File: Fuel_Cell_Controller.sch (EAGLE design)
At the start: 54 parts, among them U1 MAX232PTH

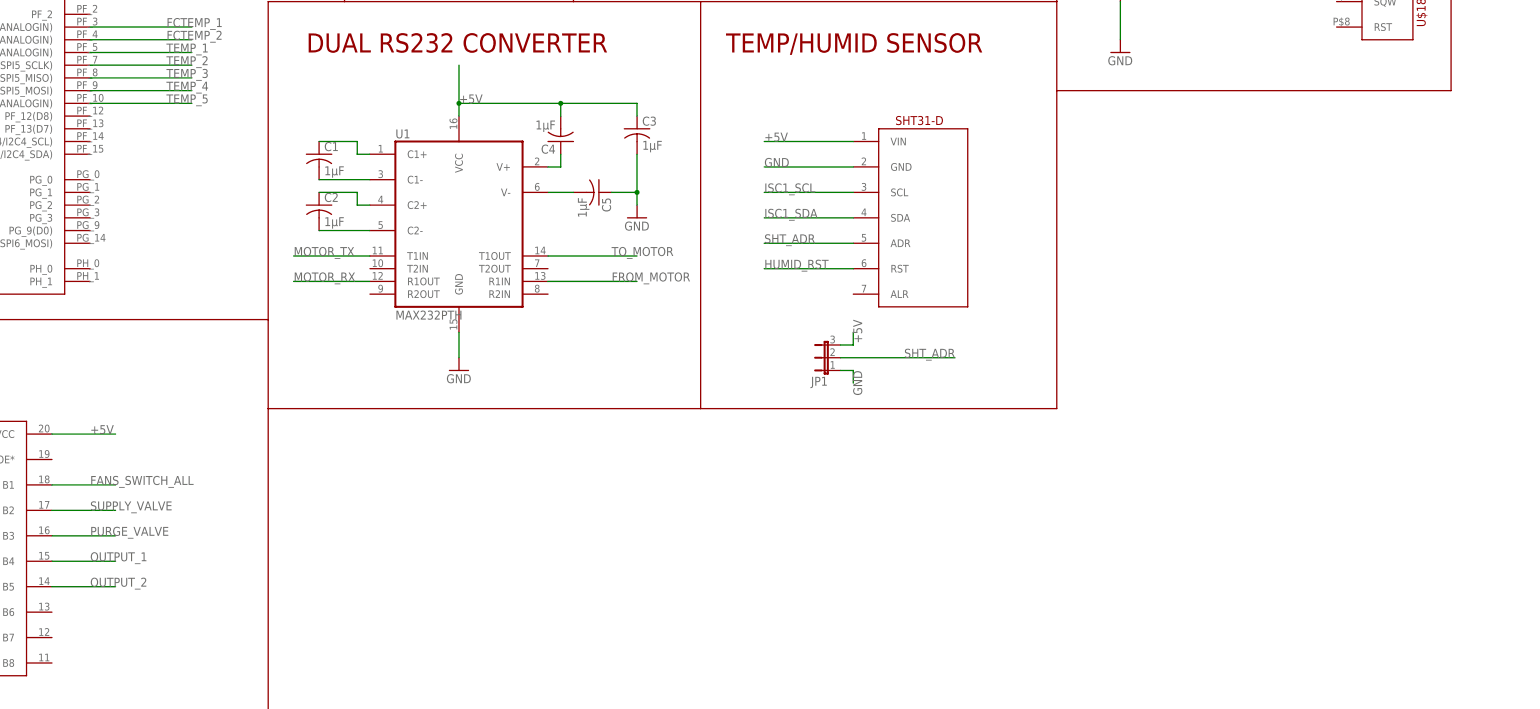
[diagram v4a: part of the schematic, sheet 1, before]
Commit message: Added ADC to schematic
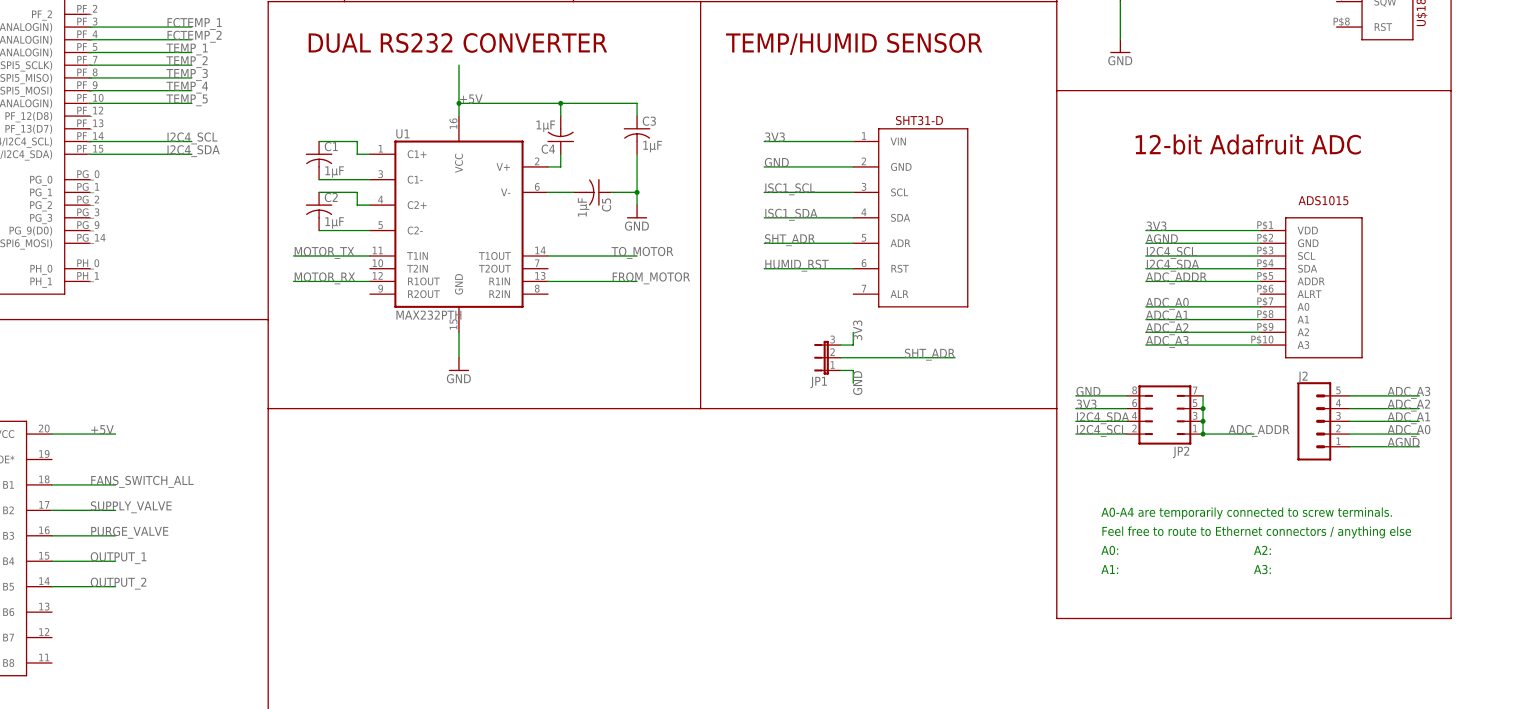
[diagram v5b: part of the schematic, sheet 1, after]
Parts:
- added J2: (no value), SparkFun-Connectors:CONN_05SCREW
- added JP2: (no value), jumper:JP4Q
- added U$19: ADS1015, FCC_parts:ADS1015
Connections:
- new net ADC_A0: J2.2, U$19.A0
- new net ADC_A1: J2.3, U$19.A1
- new net ADC_A2: J2.4, U$19.A2
- new net ADC_A3: J2.5, U$19.A3
- new net ADC_ADDR: JP2.1, JP2.3, JP2.5, JP2.7, U$19.ADDR
- new net I2C4_SCL: JP2.2, U$1.PF_14(D4/I2C4_SCL), U$19.SCL
- new net I2C4_SDA: JP2.4, U$1.PF_15(D2/I2C4_SDA), U$19.SDA
- net +5V: no longer JP1.3, SHTSENSOR.VIN
- net 3V3: now also JP1.3, JP2.6, SHTSENSOR.VIN, U$19.VDD
- net AGND: now also J2.1, U$19.GND
- net GND: now also JP2.8
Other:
- note added: "12-bit Adafruit ADC"
- note added: "A0-A4 are temporarily connected to screw terminals."
- note added: "A0:"
- note added: "A1:"
- note added: "A2:"
- note added: "A3:"
- note added: "Feel free to route to Ethernet connectors / anything else"
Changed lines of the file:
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@@
 <?xml version="1.0" encoding="utf-8"?>
 <!DOCTYPE eagle SYSTEM "eagle.dtd">
-<eagle version="8.4.0">
+<eagle version="8.3.2">
 <drawing>
 <settings>
@@
 <setting verticaltext="up"/>
 </settings>
-<grid distance="0.1" unitdist="inch" unit="inch" style="lines" multiple="1" display="no" altdistance="0.01" altunitdist="inch" altunit="inch"/>
+<grid distance="0.05" unitdist="inch" unit="inch" style="dots" multiple="1" display="no" altdistance="0.005" altunitdist="inch" altunit="inch"/>
 <layers>
 <layer number="1" name="Top" color="4" fill="1" visible="no" active="no"/>
@@
 <part name="C6" library="SparkFun-Capacitors" deviceset="CAP" device="0603-CAP"/>
 <part name="GND4" library="E-P-008-R1.2" deviceset="GND" device=""/>
+<part name="U$19" library="FCC_parts" deviceset="ADS1015" device=""/>
+<part name="JP2" library="jumper" library_urn="urn:adsk.eagle:library:252" deviceset="JP4Q" device="" package3d_urn="urn:adsk.eagle:package:15451/1"/>
+<part name="J2" library="SparkFun-Connectors" library_urn="urn:adsk.eagle:library:513" deviceset="CONN_05" device="SCREW" package3d_urn="urn:adsk.eagle:package:38112/1"/>
 </parts>
 <sheets>
@@
 <wire x1="-93.98" y1="-78.74" x2="124.46" y2="-78.74" width="0.1524" layer="94"/>
 <text x="-10.16" y="-88.9" size="3.81" layer="94">OUTPUT BUFFERS</text>
+<text x="297.18" y="-45.72" size="3.81" layer="94">12-bit Adafruit ADC</text>
+<wire x1="281.94" y1="-96.52" x2="281.94" y2="-138.43" width="0.2032" layer="94"/>
+<wire x1="281.94" y1="-138.43" x2="360.68" y2="-138.43" width="0.2032" layer="94"/>
+<wire x1="360.68" y1="-138.43" x2="360.68" y2="-33.02" width="0.2032" layer="94"/>
+<text x="290.83" y="-118.11" size="1.778" layer="91">A0-A4 are temporarily connected to screw terminals.</text>
+<text x="290.83" y="-121.92" size="1.778" layer="91">Feel free to route to Ethernet connectors / anything else</text>
+<text x="290.83" y="-125.73" size="1.778" layer="91">A0:</text>
+<text x="290.83" y="-129.54" size="1.778" layer="91">A1:</text>
+<text x="321.31" y="-125.73" size="1.778" layer="91">A2:</text>
+<text x="321.31" y="-129.54" size="1.778" layer="91">A3:</text>
 </plain>
 <instances>
@@
 <instance part="C6" gate="G$1" x="294.64" y="-12.7"/>
 <instance part="GND4" gate="1" x="294.64" y="-25.4"/>
+<instance part="U$19" gate="G$1" x="322.58" y="-81.28"/>
+<instance part="JP2" gate="B" x="303.53" y="-99.06" rot="R90"/>
+<instance part="J2" gate="G$1" x="332.74" y="-99.06"/>
 </instances>
 <busses>
@@
 <wire x1="294.64" y1="-15.24" x2="294.64" y2="-22.86" width="0.1524" layer="91"/>
 <pinref part="GND4" gate="1" pin="GND"/>
+</segment>
+<segment>
+<pinref part="JP2" gate="B" pin="8"/>
+<wire x1="295.91" y1="-93.98" x2="285.75" y2="-93.98" width="0.1524" layer="91"/>
+<label x="285.75" y="-93.98" size="1.778" layer="95"/>
 </segment>
 </net>
@@
 <wire x1="-12.7" y1="-101.6" x2="2.54" y2="-101.6" width="0.1524" layer="91"/>
 <label x="-2.54" y="-101.6" size="1.778" layer="95"/>
-</segment>
-<segment>
-<pinref part="SHTSENSOR" gate="G$1" pin="VIN"/>
-<wire x1="241.3" y1="-43.18" x2="223.52" y2="-43.18" width="0.1524" layer="91"/>
-<label x="223.52" y="-43.18" size="1.778" layer="95"/>
-</segment>
-<segment>
-<pinref part="JP1" gate="1" pin="3"/>
-<wire x1="238.76" y1="-83.82" x2="241.3" y2="-83.82" width="0.1524" layer="91"/>
-<wire x1="241.3" y1="-83.82" x2="241.3" y2="-81.28" width="0.1524" layer="91"/>
-<label x="241.3" y="-78.74" size="1.778" layer="95" rot="R270"/>
 </segment>
 <segment>
@@
 <junction x="294.64" y="2.54"/>
 </segment>
+<segment>
+<pinref part="SHTSENSOR" gate="G$1" pin="VIN"/>
+<wire x1="241.3" y1="-43.18" x2="223.52" y2="-43.18" width="0.1524" layer="91"/>
+<label x="223.52" y="-43.18" size="1.778" layer="95"/>
+</segment>
+<segment>
+<pinref part="JP1" gate="1" pin="3"/>
+<wire x1="238.76" y1="-83.82" x2="241.3" y2="-83.82" width="0.1524" layer="91"/>
+<wire x1="241.3" y1="-83.82" x2="241.3" y2="-81.28" width="0.1524" layer="91"/>
+<label x="241.3" y="-78.74" size="1.778" layer="95" rot="R270"/>
+</segment>
+<segment>
+<pinref part="U$19" gate="G$1" pin="VDD"/>
+<wire x1="322.58" y1="-60.96" x2="299.72" y2="-60.96" width="0.1524" layer="91"/>
+<label x="299.72" y="-60.96" size="1.778" layer="95"/>
+</segment>
+<segment>
+<pinref part="JP2" gate="B" pin="6"/>
+<wire x1="295.91" y1="-96.52" x2="285.75" y2="-96.52" width="0.1524" layer="91"/>
+<label x="285.75" y="-96.52" size="1.778" layer="95"/>
+</segment>
 </net>
 <net name="OPEN_RST" class="0">
@@
 <label x="-81.28" y="30.48" size="1.778" layer="95"/>
 </segment>
+<segment>
+<pinref part="U$19" gate="G$1" pin="GND"/>
+<wire x1="322.58" y1="-63.5" x2="299.72" y2="-63.5" width="0.1524" layer="91"/>
+<label x="299.72" y="-63.5" size="1.778" layer="95"/>
+</segment>
+<segment>
+<pinref part="J2" gate="G$1" pin="1"/>
+<wire x1="340.36" y1="-104.14" x2="354.33" y2="-104.14" width="0.1524" layer="91"/>
+<label x="347.98" y="-104.14" size="1.778" layer="95"/>
+</segment>
 </net>
 <net name="MASS_FLOW" class="0">
@@
 </segment>
 </net>
+<net name="ADC_A0" class="0">
+<segment>
+<pinref part="U$19" gate="G$1" pin="A0"/>
+<wire x1="322.58" y1="-76.2" x2="299.72" y2="-76.2" width="0.1524" layer="91"/>
+<label x="299.72" y="-76.2" size="1.778" layer="95"/>
+</segment>
+<segment>
+<pinref part="J2" gate="G$1" pin="2"/>
+<wire x1="340.36" y1="-101.6" x2="354.33" y2="-101.6" width="0.1524" layer="91"/>
+<label x="347.98" y="-101.6" size="1.778" layer="95"/>
+</segment>
+</net>
+<net name="ADC_A1" class="0">
+<segment>
+<pinref part="U$19" gate="G$1" pin="A1"/>
+<wire x1="322.58" y1="-78.74" x2="299.72" y2="-78.74" width="0.1524" layer="91"/>
+<label x="299.72" y="-78.74" size="1.778" layer="95"/>
+</segment>
+<segment>
+<pinref part="J2" gate="G$1" pin="3"/>
+<wire x1="340.36" y1="-99.06" x2="354.33" y2="-99.06" width="0.1524" layer="91"/>
+<label x="347.98" y="-99.06" size="1.778" layer="95"/>
+</segment>
+</net>
+<net name="ADC_A2" class="0">
+<segment>
+<pinref part="U$19" gate="G$1" pin="A2"/>
+<wire x1="322.58" y1="-81.28" x2="299.72" y2="-81.28" width="0.1524" layer="91"/>
+<label x="299.72" y="-81.28" size="1.778" layer="95"/>
+</segment>
+<segment>
+<pinref part="J2" gate="G$1" pin="4"/>
+<wire x1="340.36" y1="-96.52" x2="354.33" y2="-96.52" width="0.1524" layer="91"/>
+<label x="347.98" y="-96.52" size="1.778" layer="95"/>
+</segment>
+</net>
+<net name="ADC_A3" class="0">
+<segment>
+<pinref part="U$19" gate="G$1" pin="A3"/>
+<wire x1="322.58" y1="-83.82" x2="299.72" y2="-83.82" width="0.1524" layer="91"/>
+<label x="299.72" y="-83.82" size="1.778" layer="95"/>
+</segment>
+<segment>
+<pinref part="J2" gate="G$1" pin="5"/>
+<wire x1="340.36" y1="-93.98" x2="354.33" y2="-93.98" width="0.1524" layer="91"/>
+<label x="347.98" y="-93.98" size="1.778" layer="95"/>
+</segment>
+</net>
+<net name="I2C4_SCL" class="0">
+<segment>
+<pinref part="U$1" gate="G$1" pin="PF_14(D4/I2C4_SCL)"/>
+<wire x1="88.9" y1="-43.18" x2="109.22" y2="-43.18" width="0.1524" layer="91"/>
+<label x="104.14" y="-43.18" size="1.778" layer="95"/>
+</segment>
+<segment>
+<pinref part="U$19" gate="G$1" pin="SCL"/>
+<wire x1="322.58" y1="-66.04" x2="299.72" y2="-66.04" width="0.1524" layer="91"/>
+<label x="299.72" y="-66.04" size="1.778" layer="95"/>
+</segment>
+<segment>
+<pinref part="JP2" gate="B" pin="2"/>
+<wire x1="295.91" y1="-101.6" x2="285.75" y2="-101.6" width="0.1524" layer="91"/>
+<label x="285.75" y="-101.6" size="1.778" layer="95"/>
+</segment>
+</net>
+<net name="I2C4_SDA" class="0">
+<segment>
+<pinref part="U$1" gate="G$1" pin="PF_15(D2/I2C4_SDA)"/>
+<wire x1="88.9" y1="-45.72" x2="109.22" y2="-45.72" width="0.1524" layer="91"/>
+<label x="104.14" y="-45.72" size="1.778" layer="95"/>
+</segment>
+<segment>
+<pinref part="U$19" gate="G$1" pin="SDA"/>
+<wire x1="322.58" y1="-68.58" x2="299.72" y2="-68.58" width="0.1524" layer="91"/>
+<label x="299.72" y="-68.58" size="1.778" layer="95"/>
+</segment>
+<segment>
+<pinref part="JP2" gate="B" pin="4"/>
+<wire x1="295.91" y1="-99.06" x2="285.75" y2="-99.06" width="0.1524" layer="91"/>
+<label x="285.75" y="-99.06" size="1.778" layer="95"/>
+</segment>
+</net>
+<net name="ADC_ADDR" class="0">
+<segment>
+<pinref part="JP2" gate="B" pin="7"/>
+<pinref part="JP2" gate="B" pin="5"/>
+<wire x1="311.15" y1="-93.98" x2="311.15" y2="-96.52" width="0.1524" layer="91"/>
+<pinref part="JP2" gate="B" pin="3"/>
+<wire x1="311.15" y1="-96.52" x2="311.15" y2="-99.06" width="0.1524" layer="91"/>
+<junction x="311.15" y="-96.52"/>
+<pinref part="JP2" gate="B" pin="1"/>
+<wire x1="311.15" y1="-99.06" x2="311.15" y2="-101.6" width="0.1524" layer="91"/>
+<junction x="311.15" y="-99.06"/>
+<wire x1="311.15" y1="-101.6" x2="321.31" y2="-101.6" width="0.1524" layer="91"/>
+<junction x="311.15" y="-101.6"/>
+<label x="316.23" y="-101.6" size="1.778" layer="95"/>
+</segment>
+<segment>
+<pinref part="U$19" gate="G$1" pin="ADDR"/>
+<wire x1="322.58" y1="-71.12" x2="299.72" y2="-71.12" width="0.1524" layer="91"/>
+<label x="299.72" y="-71.12" size="1.778" layer="95"/>
+</segment>
+</net>

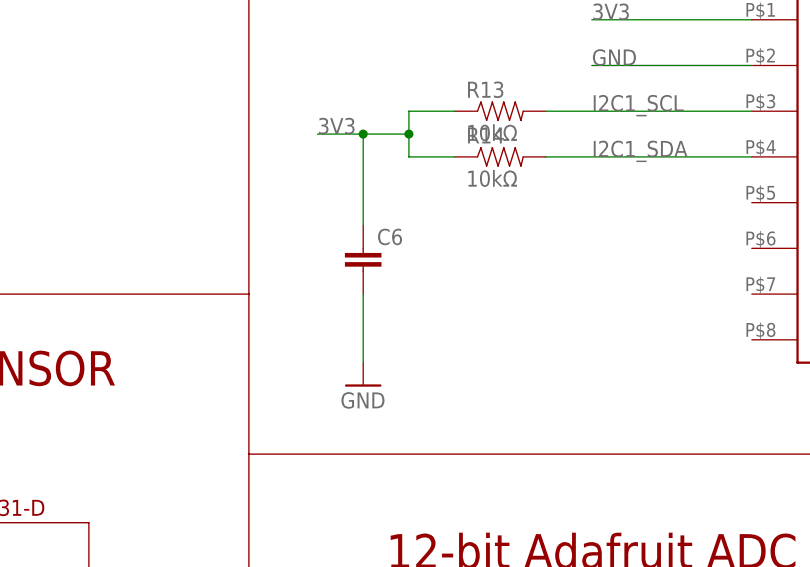
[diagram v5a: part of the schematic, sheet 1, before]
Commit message: Added value for capacitor between 3v3 and gnd on rtc
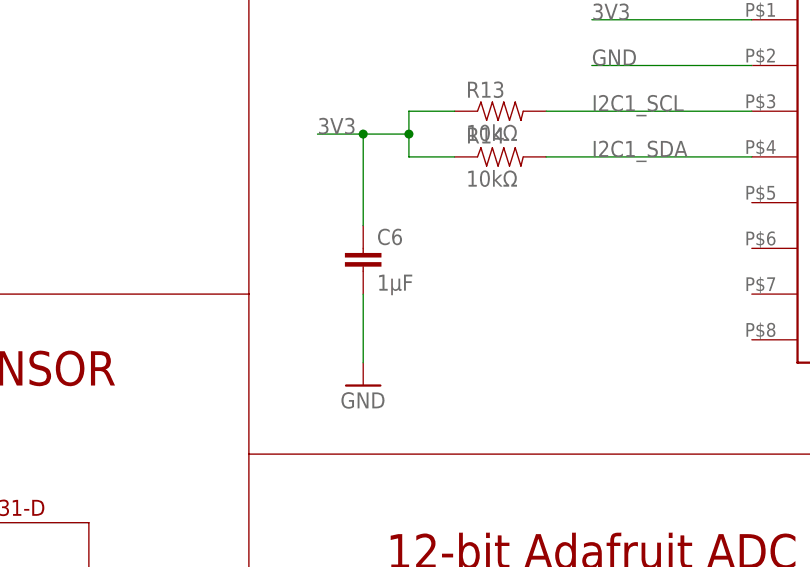
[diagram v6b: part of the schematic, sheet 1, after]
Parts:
- C6: value (none) -> 1µF
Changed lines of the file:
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@@
 <?xml version="1.0" encoding="utf-8"?>
 <!DOCTYPE eagle SYSTEM "eagle.dtd">
-<eagle version="8.3.2">
+<eagle version="8.4.1">
 <drawing>
 <settings>
@@
 <setting verticaltext="up"/>
 </settings>
-<grid distance="0.05" unitdist="inch" unit="inch" style="dots" multiple="1" display="no" altdistance="0.005" altunitdist="inch" altunit="inch"/>
+<grid distance="0.1" unitdist="inch" unit="inch" style="lines" multiple="1" display="no" altdistance="0.01" altunitdist="inch" altunit="inch"/>
 <layers>
 <layer number="1" name="Top" color="4" fill="1" visible="no" active="no"/>
@@
 <part name="R13" library="SparkFun-Resistors" deviceset="RESISTOR" device="0603" value="10kΩ"/>
 <part name="R14" library="SparkFun-Resistors" deviceset="RESISTOR" device="0603" value="10kΩ"/>
-<part name="C6" library="SparkFun-Capacitors" deviceset="CAP" device="0603-CAP"/>
+<part name="C6" library="SparkFun-Capacitors" deviceset="CAP" device="0603-CAP" value="1µF"/>
 <part name="GND4" library="E-P-008-R1.2" deviceset="GND" device=""/>
 <part name="U$19" library="FCC_parts" deviceset="ADS1015" device=""/>
